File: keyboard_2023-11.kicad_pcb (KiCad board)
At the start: 2 copper layers, 126 x 98 mm, 74 parts, among them J1 Conn_01x04, J10 Conn_01x01_Socket, J11 Conn_01x07_Socket, J2 Conn_01x04_Socket, J3 Conn_01x07_Socket, J4 Conn_01x07_Pin, J5 Conn_01x01_Socket, J6 Conn_01x01_Socket, J7 Conn_01x01_Socket, J8 Conn_01x01_Socket, J9 Conn_01x01_Socket, SW1 SW_Push, SW10 SW_Push, SW11 SW_Push, SW12 SW_Push, SW13 SW_Push, SW14 SW_Push, SW15 SW_Push, SW16 SW_Push, SW17 SW_Push, SW18 SW_Push, SW19 SW_Push, SW2 SW_Push, SW20 SW_Push, SW21 SW_Push, SW22 SW_Push, SW23 SW_Push, SW24 SW_Push, SW3 SW_Push, SW4 SW_Push, SW5 SW_Push, SW6 SW_Push, SW7 SW_Push, SW8 SW_Push, SW9 SW_Push, U1 MCP23017_SO, U2 MCP23017_SO

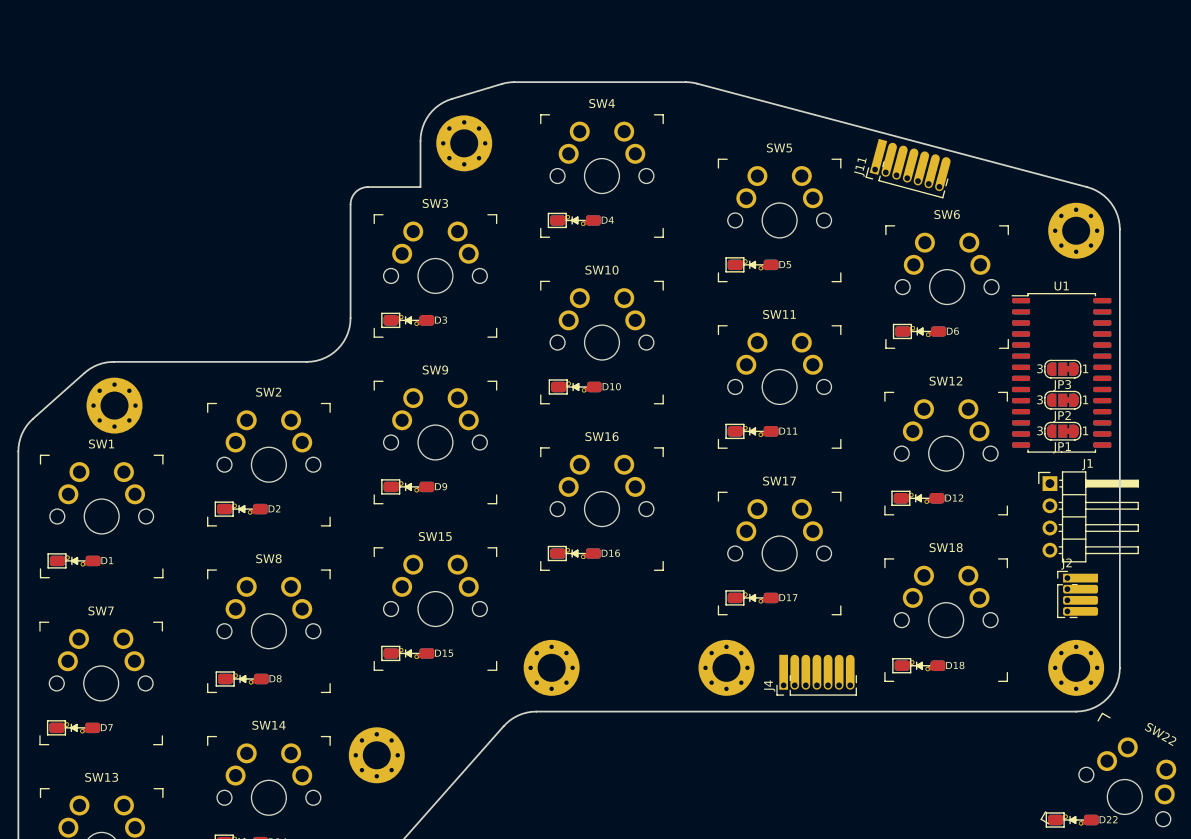
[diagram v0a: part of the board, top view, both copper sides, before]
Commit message: PCB: move ioexpander from right-edge to up-left corner
removing/shuffeling mounting holes, to remove pcb area that might interfere with monoblock design; or possibly with electronics placed between the two halves
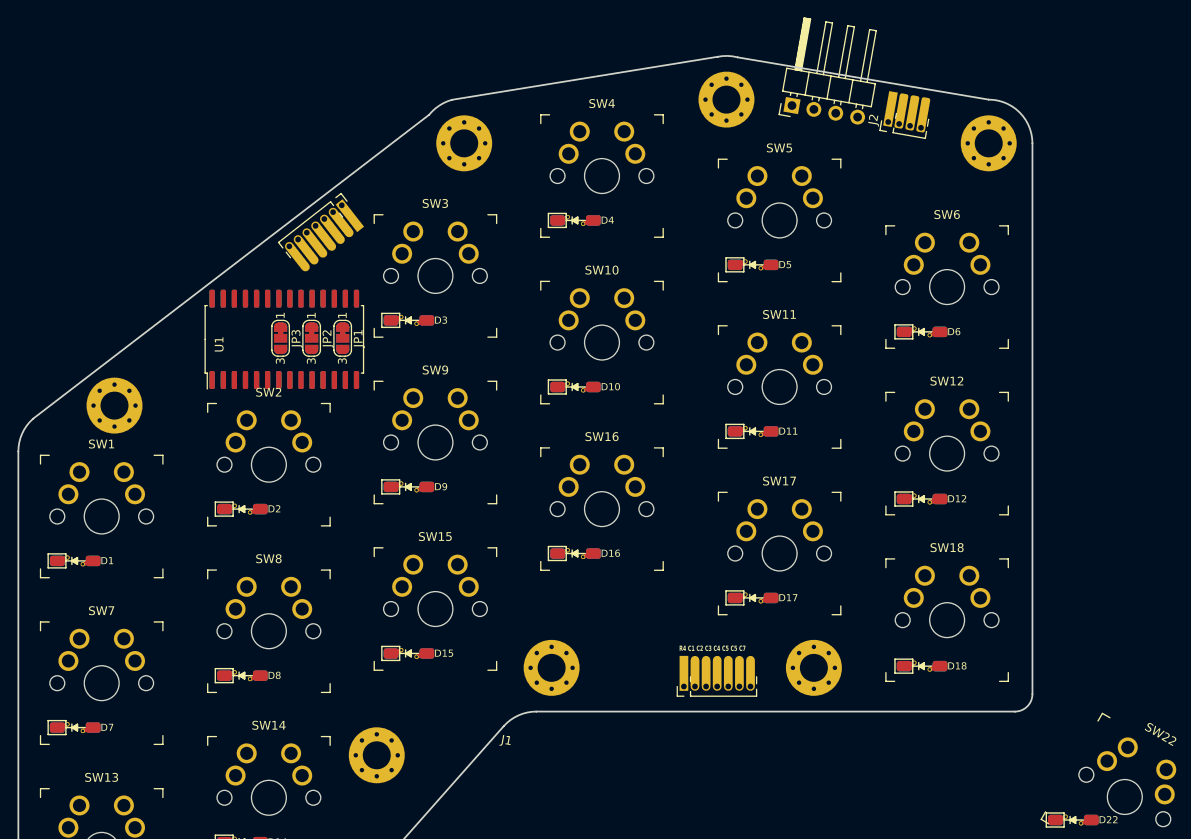
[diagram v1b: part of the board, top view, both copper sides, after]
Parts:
- moved JP3 89.5 mm to (59.0, 52.3), turned to -90 degrees
- moved JP4 89.5 mm to (59.0, 52.3), turned to -90 degrees
- moved U1 89.0 mm to (59.4, 52.4), turned to 90 degrees
- moved U2 89.0 mm to (59.4, 52.4), turned to -90 degrees
- moved JP2 86.2 mm to (62.5, 52.3), turned to -90 degrees
- moved JP5 86.2 mm to (62.5, 52.3), turned to -90 degrees
- moved JP1 83.1 mm to (66.1, 52.3), turned to -90 degrees
- moved JP6 83.1 mm to (66.1, 52.3), turned to -90 degrees
- moved J11 61.1 mm to (66.0, 37.1), turned to -52 degrees
- moved H5 60.8 mm to (140.0, 30.0)
- moved J2 56.1 mm to (128.5, 27.6), turned to 80 degrees
- moved J1 52.3 mm to (117.5, 25.7), turned to 80 degrees
- moved H1 42.7 mm to (110.0, 25.0)
- moved J4 11.4 mm to (105.1, 92.1)
- moved H6 10.0 mm to (120.0, 90.0)
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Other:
- board size 126 x 98 mm -> 116 x 101 mm
- board text added: "R4 C1 C2 C3 C4 C5 C5 C7"

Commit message: routed 90%
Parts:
- removed J10, J5, J6, J7, J8, J9: Conn_01x01_Socket, project-local:PinHeader_1x01_P2.54mm_Vertical
- moved J3 53.5 mm to (186.5, 98.5)
- moved J11 10.6 mm to (59.0, 45.0), turned to 128 degrees
- moved JP6 7.10 mm to (59.0, 52.3)
- moved JP4 7.00 mm to (66.0, 52.3)
- moved JP1 0.10 mm to (66.0, 52.3)
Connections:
- JP1 pad 2: Net-(JP1-C) -> A0
- JP2 pad 2: Net-(JP2-C) -> A1
- JP3 pad 2: Net-(JP3-C) -> A2
- JP4 pad 2: Net-(JP4-C) -> A0
- JP5 pad 2: Net-(JP5-C) -> A1
- JP6 pad 2: Net-(JP6-C) -> A2
- U1 pad 15: Net-(JP1-C) -> A0
- U1 pad 16: Net-(JP2-C) -> A1
- U1 pad 17: Net-(JP3-C) -> A2
- U2 pad 15: Net-(JP4-C) -> A0
- U2 pad 16: Net-(JP5-C) -> A1
- U2 pad 17: Net-(JP6-C) -> A2
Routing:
- net GND: track 0.00 -> 384.4 mm, vias 0 -> 4
- net ROW3: track 0.00 -> 196.7 mm, vias 0 -> 4
- net COL6: track 0.00 -> 186.8 mm, vias 0 -> 2
- net ROW2: track 0.00 -> 181.6 mm, vias 0 -> 1
- net COL1: track 0.00 -> 164.2 mm, vias 0 -> 2
- net ROW1: track 0.00 -> 155.0 mm, vias 0 -> 1
- net COL5: track 0.00 -> 148.5 mm, vias 0 -> 4
- net COL2: track 0.00 -> 141.7 mm, vias 0 -> 1
- net VDD: track 0.00 -> 136.5 mm, vias 0 -> 8
- net COL4: track 0.00 -> 135.8 mm, vias 0 -> 4
- net COL3: track 0.00 -> 122.6 mm, vias 0 -> 1
- net ROW4: track 0.00 -> 85.6 mm, vias 0 -> 4
- net SCK: track 0.00 -> 79.1 mm
- net SDA: track 0.00 -> 78.6 mm
- net Net-(D3-K): track 0.00 -> 19.4 mm
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
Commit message: snapshot
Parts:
- SW1, SW10, SW11, SW12, SW13, SW14, SW15, SW16, SW17, SW18, SW19, SW2, SW20, SW21, SW22, SW23, SW24, SW3, SW4, SW5, SW6, SW7, SW8, SW9: footprint keyswitches:SW_MX_reversible -> project-local:SW_MX_reversible
- moved J11 9.82 mm to (64.5, 36.9), turned to -52 degrees
- moved D23 2.15 mm to (167.0, 120.0), turned to -45 degrees
- moved D24 1.30 mm to (180.7, 135.8), turned to -60 degrees
- moved D22 0.86 mm to (150.4, 107.8), turned to -30 degrees
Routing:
- net Net-(D19-A): track 0.00 -> 166.8 mm
- net Net-(J3-Pin_2): track 0.00 -> 81.7 mm
- net Net-(J3-Pin_3): track 0.00 -> 75.5 mm, vias 0 -> 1
- net Net-(J3-Pin_7): track 0.00 -> 40.8 mm
- net Net-(J3-Pin_4): track 0.00 -> 38.5 mm
- net ROW4: track 85.6 -> 123.5 mm, vias 4 -> 3
- net Net-(J3-Pin_5): track 0.00 -> 35.5 mm
- net COL5: track 148.5 -> 182.8 mm
- net ROW5: track 0.00 -> 33.6 mm, vias 0 -> 2
- net COL6: track 186.8 -> 219.5 mm
- net COL8: track 0.00 -> 30.9 mm, vias 0 -> 1
- net SCK: track 79.1 -> 109.1 mm, vias 0 -> 1
- net ROW6: track 0.00 -> 28.9 mm, vias 0 -> 2
- net Net-(J3-Pin_6): track 0.00 -> 27.3 mm
- net SDA: track 78.6 -> 105.6 mm, vias 0 -> 1
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- added copper zone on B.Cu, net GND
- added copper zone on F.Cu, net GND

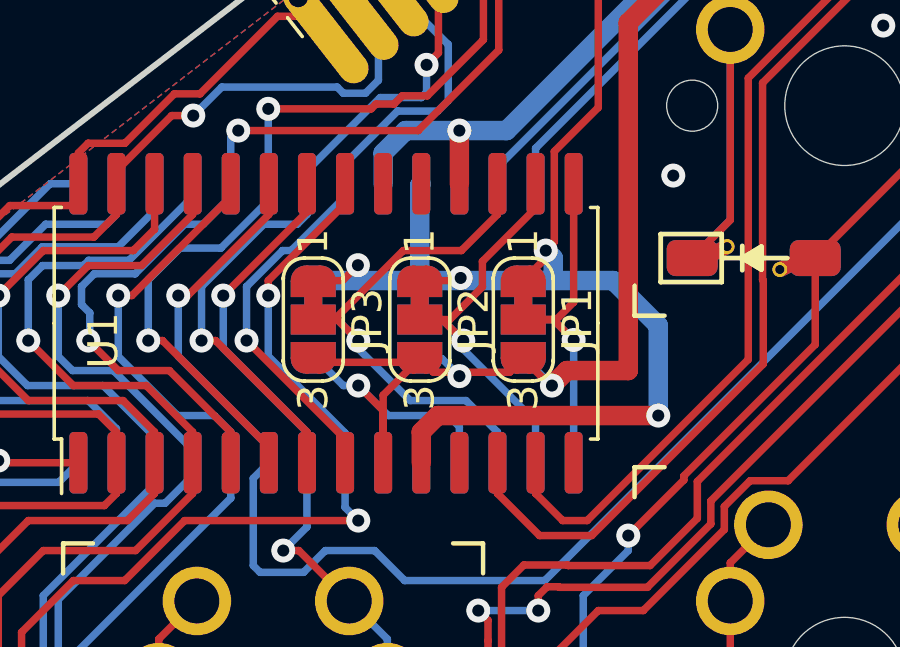
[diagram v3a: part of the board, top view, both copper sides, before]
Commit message: fix solder jumpers
front/back io-expander need sepparate jumpers, as the already have preset values which might conflict with user selection = create a short.
switch solder jumpers to opposite side of board of the coresponding io-expander
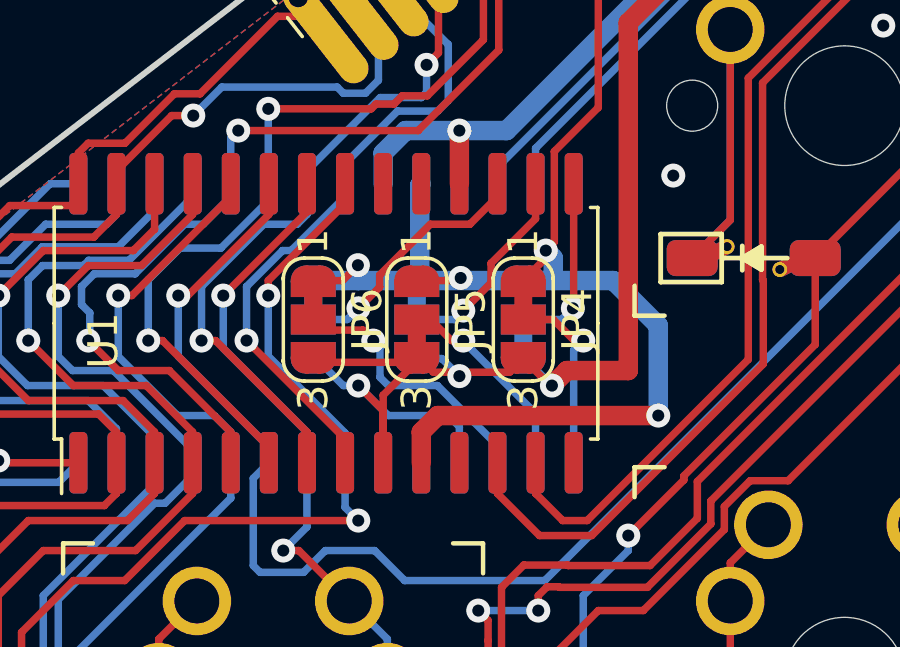
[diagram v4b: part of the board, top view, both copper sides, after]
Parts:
- JP1: footprint Jumper:SolderJumper-3_P1.3mm_Bridged12_RoundedPad1.0x1.5mm_NumberLabels -> project-local:SolderJumper-3_P1.3mm_Bridged23_RoundedPad1.0x1.5mm_NumberLabels; moved to B.Cu
- JP2, JP3: moved to B.Cu
- JP4, JP6: moved to F.Cu
- JP5: footprint Jumper:SolderJumper-3_P1.3mm_Bridged12_RoundedPad1.0x1.5mm_NumberLabels -> project-local:SolderJumper-3_P1.3mm_Bridged23_RoundedPad1.0x1.5mm_NumberLabels; moved to F.Cu
- moved JP5 0.10 mm to (62.5, 52.3)
- moved JP2 0.10 mm to (62.5, 52.3)
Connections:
- JP1 pad 2: A0 -> Net-(JP1-C)
- JP2 pad 2: A1 -> Net-(JP2-C)
- JP3 pad 2: A2 -> Net-(JP3-C)
- JP4 pad 2: A0 -> Net-(JP4-C)
- JP5 pad 2: A1 -> Net-(JP5-C)
- JP6 pad 2: A2 -> Net-(JP6-C)
- U1 pad 15: A0 -> Net-(JP1-C)
- U1 pad 16: A1 -> Net-(JP2-C)
- U1 pad 17: A2 -> Net-(JP3-C)
- U2 pad 15: A0 -> Net-(JP4-C)
- U2 pad 16: A1 -> Net-(JP5-C)
- U2 pad 17: A2 -> Net-(JP6-C)
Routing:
- net A2: track 19.3 -> 0.00 mm, vias 1 -> 0
- net A1: track 15.3 -> 0.00 mm, vias 1 -> 0
- net A0: track 14.1 -> 0.00 mm, vias 1 -> 0
- net Net-(JP6-C): track 0.00 -> 9.04 mm, vias 0 -> 1
- net Net-(JP3-C): track 0.00 -> 8.50 mm, vias 0 -> 1
- net Net-(JP5-C): track 0.00 -> 6.91 mm, vias 0 -> 1
- net Net-(JP2-C): track 0.00 -> 6.90 mm, vias 0 -> 1
- net Net-(JP4-C): track 0.00 -> 6.50 mm, vias 0 -> 1
- net Net-(JP1-C): track 0.00 -> 5.97 mm, vias 0 -> 1

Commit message: snapshot
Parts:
- moved SW24 122.3 mm to (267.8, 44.4), turned to -30 degrees
- moved D24 120.7 mm to (262.8, 47.3), turned to -30 degrees
- moved SW23 110.9 mm to (247.3, 35.9), turned to -15 degrees
- moved D23 110.0 mm to (243.0, 40.5), turned to -15 degrees
- moved D22 100.3 mm to (222.6, 38.2), turned to 0 degrees
- moved SW22 100.2 mm to (225.5, 33.0), turned to 0 degrees
- moved J3 74.6 mm to (206.2, 26.5)
- moved D21 69.9 mm to (178.3, 43.6)
- moved SW21 69.9 mm to (181.5, 38.3)
- moved D19 69.9 mm to (197.2, 62.4)
- moved D20 69.9 mm to (178.5, 62.4)
- moved SW19 69.9 mm to (200.5, 57.3)
- moved SW20 69.9 mm to (181.5, 57.3)
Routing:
- net Net-(D19-A): track 166.8 -> 46.6 mm
- net Net-(J3-Pin_2): track 81.7 -> 3.07 mm
- net Net-(J3-Pin_3): track 75.5 -> 3.07 mm, vias 1 -> 0
- net Net-(J3-Pin_7): track 40.8 -> 0.00 mm
- net Net-(J3-Pin_5): track 35.5 -> 0.00 mm
- net Net-(J3-Pin_4): track 38.5 -> 9.40 mm
- net Net-(J3-Pin_6): track 27.3 -> 0.00 mm
- net Net-(D23-K): track 11.6 -> 0.00 mm
- net Net-(D22-K): track 11.2 -> 0.00 mm
- net Net-(D24-K): track 11.2 -> 0.00 mm
- net COL1: track 164.2 -> 166.4 mm
- net COL2: track 118.4 -> 119.6 mm
- net ROW3: track 211.5 -> 212.1 mm
- net GND: vias 27 -> 29
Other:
- board size 116 x 101 mm -> 253.3 x 100.4 mm

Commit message: snapshot
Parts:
- added svg2mod: G***, project-local:logo, F.Cu at (78.2, 97.8)
- added svg2mod: G***, project-local:logo, B.Cu at (78.2, 97.8)
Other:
- board text added: "2023-12"

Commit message: ready for ORDER
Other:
- board text added: "Gnd R5 R6 R7 R8 C7 C8"
- board text added: "R4 C1 C2 C3 C4 C5 C6 C7"
- board text added: "SCK SDA Vdd Gnd"
- board text removed: "R4 C1 C2 C3 C4 C5 C5 C7"
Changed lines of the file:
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@@
   (gr_line (start 111.282186 20.167192) (end 140.4 25)
     (stroke (width 0.2) (type default)) (layer "Edge.Cuts"))
-  (gr_text "R4 C1 C2 C3 C4 C5 C5 C7\n" (at 104.591968 88.13) (layer "F.SilkS")
-    (effects (font (size 0.6 0.4) (thickness 0.1) bold) (justify left bottom))
+  (gr_text "SCK\nSDA\nVdd\nGnd" (at 133 30.2 80) (layer "B.SilkS")
+    (effects (font (size 1 1) (thickness 0.15)) (justify left bottom mirror))
+  )
+  (gr_text "Gnd\nR5\nR6\nR7\nR8\nC7\nC8" (at 61.2 46.2 308) (layer "B.SilkS")
+    (effects (font (size 0.8 0.6) (thickness 0.1) bold) (justify left bottom mirror))
+  )
+  (gr_text "R4\nC1\nC2\nC3\nC4\nC5\nC6\nC7" (at 113.2 87 90) (layer "B.SilkS")
+    (effects (font (size 0.7 0.6) (thickness 0.1) bold) (justify left bottom mirror))
+  )
+  (gr_text "Gnd\nR5\nR6\nR7\nR8\nC7\nC8" (at 60.4 45.2 308) (layer "F.SilkS")
+    (effects (font (size 0.8 0.6) (thickness 0.1) bold) (justify left bottom))
+  )
+  (gr_text "R4 \nC1 \nC2 \nC3 \nC4 \nC5\nC6\nC7" (at 113.2 88.2 90) (layer "F.SilkS")
+    (effects (font (size 0.7 0.6) (thickness 0.1) bold) (justify left bottom))
+  )
+  (gr_text "SCK\nSDA\nVdd\nGnd" (at 132.4 33 80) (layer "F.SilkS")
+    (effects (font (size 1 1) (thickness 0.15)) (justify left bottom))
   )
   (gr_text "2023-12" (at 131.8 36.2) (layer "F.Mask")
@@
     (polygon
       (pts
-        (xy 50.5 48.5)
-        (xy 68.5 48.5)
-        (xy 68.5 56)
-        (xy 50.5 56)
+        (xy 50.5 46.6)
+        (xy 68.6 46.6)
+        (xy 68.5 58.4)
+        (xy 50.6 58.4)
       )
     )
-  )
-  (zone (net 0) (net_name "") (layers "F&B.Cu" "*.Adhes" "*.Paste" "*.SilkS" "*.Mask") (hatch full 0.5)
-    (connect_pads (clearance 0))
-    (min_thickness 0.25) (filled_areas_thickness no)
-    (keepout (tracks not_allowed) (vias not_allowed) (pads not_allowed) (copperpour not_allowed) (footprints not_allowed))
-    (fill (thermal_gap 0.5) (thermal_bridge_width 0.5))
-    (polygon
-      (pts
-        (xy 160 12.8)
-        (xy 159.8 96.2)
-        (xy 288.4 96)
-        (xy 287.2 13.8)
-      )
-    )

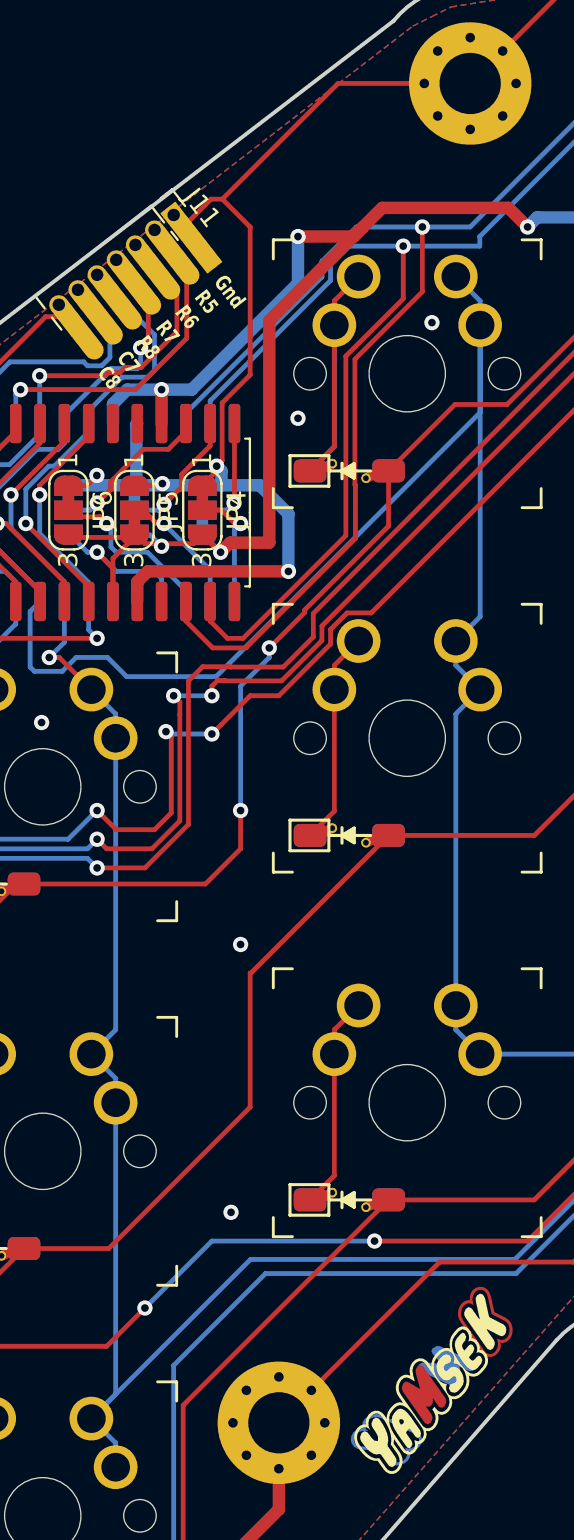
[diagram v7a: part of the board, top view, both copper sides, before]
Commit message: better solder jumpers?
adding a solder mask cutout where the pads are default-connected, to better see which part needs to be scrached out

Signed-off-by: Johannes <you@example.com>
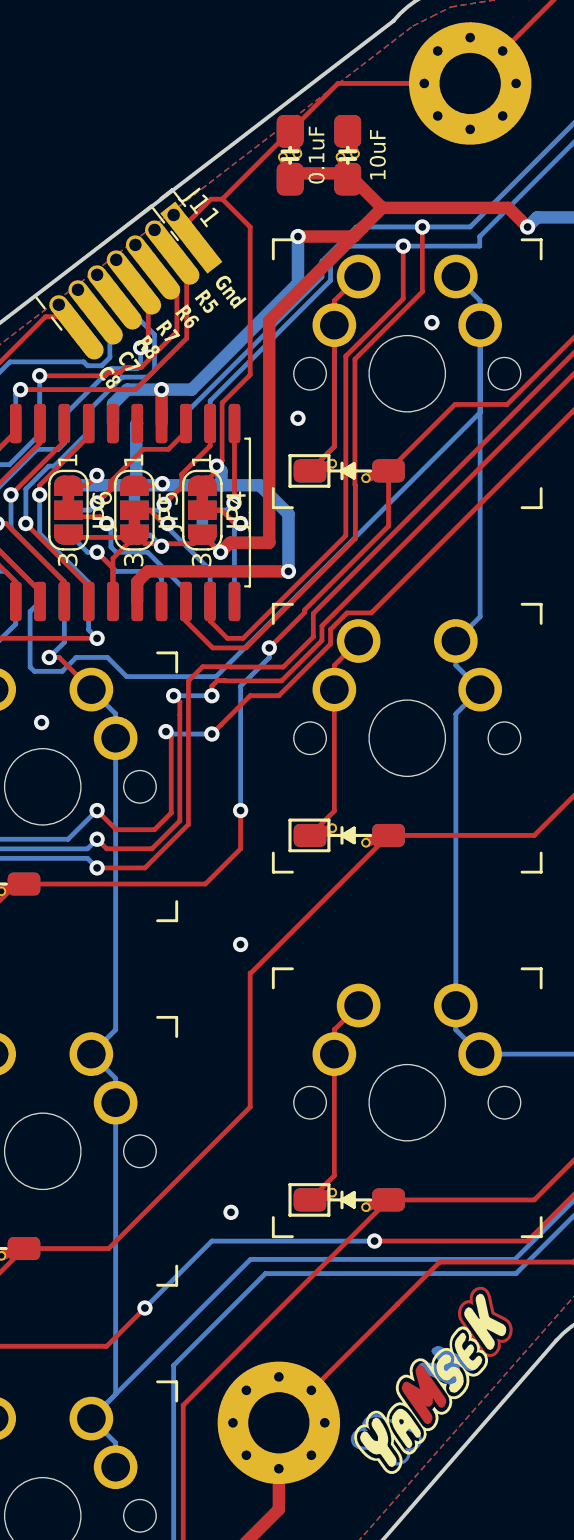
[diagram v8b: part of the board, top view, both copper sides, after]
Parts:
- added C1: 0.1uF, reversible-kicad:C-0805_2012Metric, F.Cu at (70.6, 33.8)
- added C2: 10uF, reversible-kicad:C-0805_2012Metric, F.Cu at (73.6, 33.8)
- H8, H9: renamed from svg2mod; value G*** -> Logo
- JP2, JP3, JP4, JP6: footprint Jumper:SolderJumper-3_P1.3mm_Bridged12_RoundedPad1.0x1.5mm_NumberLabels -> project-local:SolderJumper-3_P1.3mm_Bridged12_RoundedPad1.0x1.5mm_NumberLabels
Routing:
- net VDD: track 142.9 -> 148.5 mm
- net GND: track 388.9 -> 390.8 mm
